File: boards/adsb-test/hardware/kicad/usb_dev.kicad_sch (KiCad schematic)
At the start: 108 parts, among them J1001 Dev USB-C, Q1001 MMBT3904, Q1002 MMBT3904, Q1003 MMBT3904, Q1004 MMBT3904, SW1001 BOOTSEL (programmer), U1001 USBLC6-2SC6, U1002 AP2112K-3.3, U1003 USB2514B, U1004 FT2232HL, U1005 93LC56B, U1006 74LVC1G07, U1007 74LVC1G125, U1008 74LVC1G07, U1009 74LVC1G125, U1010 RP2040, U1011 W25Q16JVSS, U1012 74LVC1G125, U1013 74LVC1G125, U1014 74LVC1G125, U1015 74LVC1G125, Y1001 24MHz, Y1002 12MHz, Y1003 12MHz

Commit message: ADSB_Test: User USB-C on its own sheet, RP2040 GPIO header + optional I2C, shunt/PWR_FLAG text fixed
Co-Authored-By: Claude Opus 5.5 <noreply@anthropic.com>
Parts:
- added J1003: RP2040 GPIO (pins DNP), Connector_PinHeader_2.54mm:PinHeader_2x14_P2.54mm_Vertical, symbol Connector_Generic:Conn_02x14_Odd_Even
- added R1041, R1042: 0R, Resistor_SMD:R_0805_2012Metric_Pad1.20x1.40mm_HandSolder, symbol Device:R
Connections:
- net 3V3_DEV: now also J1003.1 (Pin_1)
- net GND: now also J1003.27 (Pin_27), J1003.28 (Pin_28)
- net RP_GPIO8: now reaches U1010.11 (GPIO8)
- net RP_GPIO8: now also J1003.10 (Pin_10)
- net RP_GPIO9: now reaches U1010.12 (GPIO9)
- net RP_GPIO9: now also J1003.11 (Pin_11)
- net RP_GPIO10: now reaches U1010.13 (GPIO10)
- net RP_GPIO10: now also J1003.12 (Pin_12)
- net RP_GPIO11: now reaches U1010.14 (GPIO11)
- net RP_GPIO11: now also J1003.13 (Pin_13)
- net RP_GPIO12: now reaches U1010.15 (GPIO12)
- net RP_GPIO12: now also J1003.14 (Pin_14)
- net RP_GPIO13: now reaches U1010.16 (GPIO13)
- net RP_GPIO13: now also J1003.15 (Pin_15)
- net RP_GPIO14: now reaches U1010.17 (GPIO14)
- net RP_GPIO14: now also J1003.16 (Pin_16)
- net RP_GPIO15: now reaches U1010.18 (GPIO15)
- net RP_GPIO15: now also J1003.17 (Pin_17)
- net RP_GPIO0: now reaches U1010.2 (GPIO0)
- net RP_GPIO0: now also J1003.2 (Pin_2), R1041.1
- net RP_GPIO17: now reaches U1010.28 (GPIO17)
- net RP_GPIO17: now also J1003.18 (Pin_18)
- net RP_GPIO18: now reaches U1010.29 (GPIO18)
- net RP_GPIO18: now also J1003.19 (Pin_19)
- net RP_GPIO1: now reaches U1010.3 (GPIO1)
- net RP_GPIO1: now also J1003.3 (Pin_3), R1042.1
- net RP_GPIO19: now reaches U1010.30 (GPIO19)
- net RP_GPIO19: now also J1003.20 (Pin_20)
- net RP_GPIO20: now reaches U1010.31 (GPIO20)
- net RP_GPIO20: now also J1003.21 (Pin_21)
- net RP_GPIO21: now reaches U1010.32 (GPIO21)
- net RP_GPIO21: now also J1003.22 (Pin_22)
- net RP_GPIO22: now reaches U1010.34 (GPIO22)
- net RP_GPIO22: now also J1003.23 (Pin_23)
- net RP_GPIO23: now reaches U1010.35 (GPIO23)
- net RP_GPIO23: now also J1003.24 (Pin_24)
- net RP_GPIO24: now reaches U1010.36 (GPIO24)
- net RP_GPIO24: now also J1003.25 (Pin_25)
- net RP_GPIO25: now reaches U1010.37 (GPIO25)
- net RP_GPIO25: now also J1003.26 (Pin_26)
- net RP_GPIO2: now reaches U1010.4 (GPIO2)
- net RP_GPIO2: now also J1003.4 (Pin_4)
- net RP_GPIO3: now reaches U1010.5 (GPIO3)
- net RP_GPIO3: now also J1003.5 (Pin_5)
- net RP_GPIO4: now reaches U1010.6 (GPIO4)
- net RP_GPIO4: now also J1003.6 (Pin_6)
- net RP_GPIO5: now reaches U1010.7 (GPIO5)
- net RP_GPIO5: now also J1003.7 (Pin_7)
- net RP_GPIO6: now reaches U1010.8 (GPIO6)
- net RP_GPIO6: now also J1003.8 (Pin_8)
- net RP_GPIO7: now reaches U1010.9 (GPIO7)
- net RP_GPIO7: now also J1003.9 (Pin_9)
- new net I2C_SCL: R1042.2
- new net I2C_SDA: R1041.2
- no-connect marks 66 -> 41

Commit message: ADSB_Test: Dev port split over three A3 sheets; old note boxes replaced with short current notes
Co-Authored-By: Claude Opus 5.5 <noreply@anthropic.com>
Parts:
- removed C1013, C1014, C1015, C1016, C1024, C1025, C1026, C1027, C1028, C1029, C1030, C1031, C1032, C1033, C1034, C1035, C1036, C1037: 100nF, Capacitor_SMD:C_0805_2012Metric_Pad1.18x1.45mm_HandSolder, symbol Device:C
- removed C1017: 4.7uF, Capacitor_SMD:C_0805_2012Metric_Pad1.18x1.45mm_HandSolder, symbol Device:C
- removed C1018, C1019, C1020, C1021: 27pF, Capacitor_SMD:C_0805_2012Metric_Pad1.18x1.45mm_HandSolder, symbol Device:C
- removed C1022, C1023: 1uF, Capacitor_SMD:C_0805_2012Metric_Pad1.18x1.45mm_HandSolder, symbol Device:C
- removed D1001: 1N4148W, Diode_SMD:D_SOD-123, symbol Device:D
- removed D1002: WS2812B, LED_SMD:LED_WS2812B_PLCC4_5.0x5.0mm_P3.2mm, symbol LED:WS2812B
- removed J1003: RP2040 GPIO (pins DNP), Connector_PinHeader_2.54mm:PinHeader_2x14_P2.54mm_Vertical, symbol Connector_Generic:Conn_02x14_Odd_Even
- removed Q1001, Q1002, Q1003, Q1004: MMBT3904, Package_TO_SOT_SMD:SOT-23_Handsoldering, symbol Transistor_BJT:MMBT3904
- removed R1014: 12k 1%, Resistor_SMD:R_0805_2012Metric_Pad1.20x1.40mm_HandSolder, symbol Device:R
- removed R1015, R1017, R1018, R1019, R1020, R1021, R1022, R1023, R1024, R1025, R1033, R1034, R1039: 10k, Resistor_SMD:R_0805_2012Metric_Pad1.20x1.40mm_HandSolder, symbol Device:R
- removed R1016: 2.2k, Resistor_SMD:R_0805_2012Metric_Pad1.20x1.40mm_HandSolder, symbol Device:R
- removed R1030, R1031: 27R, Resistor_SMD:R_0805_2012Metric_Pad1.20x1.40mm_HandSolder, symbol Device:R
- removed R1032, R1035: 1k, Resistor_SMD:R_0805_2012Metric_Pad1.20x1.40mm_HandSolder, symbol Device:R
- removed R1036: 330R, Resistor_SMD:R_0805_2012Metric_Pad1.20x1.40mm_HandSolder, symbol Device:R
- removed R1037, R1038, R1041, R1042: 0R, Resistor_SMD:R_0805_2012Metric_Pad1.20x1.40mm_HandSolder, symbol Device:R
- removed R1040: 100k, Resistor_SMD:R_0805_2012Metric_Pad1.20x1.40mm_HandSolder, symbol Device:R
- removed SW1001: BOOTSEL (programmer), Button_Switch_THT:SW_PUSH_6mm, symbol Switch:SW_Push
- removed TP1003: RP_SWCLK, TestPoint:TestPoint_Pad_D1.5mm, symbol Connector:TestPoint
- removed TP1004: RP_SWDIO, TestPoint:TestPoint_Pad_D1.5mm, symbol Connector:TestPoint
- removed TP1005: RP_RUN, TestPoint:TestPoint_Pad_D1.5mm, symbol Connector:TestPoint
- removed TP1006: FT_A_DTR, TestPoint:TestPoint_Pad_D1.5mm, symbol Connector:TestPoint
- removed TP1007: FT_A_RTS, TestPoint:TestPoint_Pad_D1.5mm, symbol Connector:TestPoint
- removed TP1008: FT_B_DTR, TestPoint:TestPoint_Pad_D1.5mm, symbol Connector:TestPoint
- removed TP1009: FT_B_RTS, TestPoint:TestPoint_Pad_D1.5mm, symbol Connector:TestPoint
- removed U1004: FT2232HL, Package_QFP:LQFP-64_10x10mm_P0.5mm, symbol Interface_USB:FT2232HL
- removed U1005: 93LC56B, Package_SO:SOIC-8_3.9x4.9mm_P1.27mm, symbol Memory_EEPROM:93LCxxB
- removed U1006, U1008: 74LVC1G07, Package_TO_SOT_SMD:SOT-23-5_HandSoldering, symbol 74xGxx:74LVC1G07
- removed U1007, U1009, U1012, U1013, U1014, U1015: 74LVC1G125, Package_TO_SOT_SMD:SOT-23-5_HandSoldering, symbol 74xGxx:74LVC1G125
- removed U1010: RP2040, ADSB_Test:QFN-56-1EP_7x7mm_P0.4mm_EP3.2x3.2mm_HandSolder, symbol MCU_RaspberryPi:RP2040
- removed U1011: W25Q16JVSS, Package_SO:SOIC-8_5.3x5.3mm_P1.27mm, symbol Memory_Flash:W25Q16JVSS
- removed Y1002, Y1003: 12MHz, Crystal:Crystal_SMD_5032-2Pin_5.0x3.2mm_HandSoldering, symbol Device:Crystal
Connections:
- no-connect marks 41 -> 10
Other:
- note added: "DEV PORT, page 1 of 3: Dev USB-C -> USBLC6 -> USB2514B hub (strap defaults, bus powered). Own 3V3_DEV domain from Dev VBUS (AP2112K), so the Dev port works with the target unpowered. Downstream: DN1 P4 USB-Serial/JTAG | DN2 disabled (the C5 USB pins are its SDIO bus) | DN3 FT2232H -> page 'Dev UARTs' | DN4 RP2040 -> page 'Dev m1421 Programmer'."
- note removed: "DEV PORT (own 3V3_DEV domain from Dev VBUS; works with the target unpowered): USB-C -> USBLC6 -> USB2514B hub (strap defaults, bus powered). DN1 P4 USB-Serial/JTAG, DN2 disabled (C5 USB = SDIO pins), DN3 FT2232HL: A = P4 UART0, B = C5 UART0, DTR/RTS -> MMBT3904 pairs (esptool auto-reset) on P4_EN/BOOT and C5_EN/BOOT. DN4 RP2040 + W25Q16 running the STOCK ADSBee 1421 Programmer: GPIO26 ~SRST, 27 S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"
- title: ADSB_Test - USB Dev -> ADSB_Test - Dev USB Hub

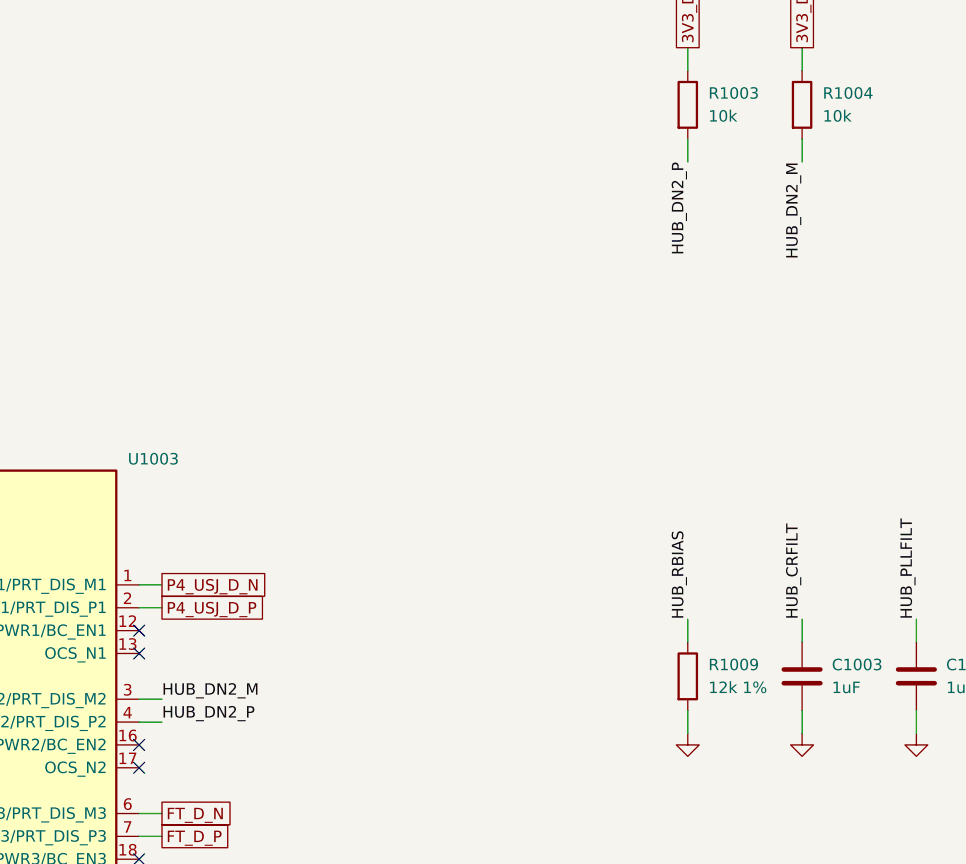
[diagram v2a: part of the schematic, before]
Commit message: ADSB_Test: Ethernet pairs named _P/_N, net classes restored in the project
- ETH_TXP/TXN/RXP/RXN -> ETH_TX_P/_N, ETH_RX_P/_N; HUB_DN2_M -> HUB_DN2_N.
- gen_pcb.py: pcbnew SaveBoard rewrote ADSB_Test.kicad_pro with empty
  net_settings, so every impedance class had been lost since the PCB start.
  Net settings are now kept across the save; 29 nets back in their classes.

Co-Authored-By: Claude Opus 5.5 <noreply@anthropic.com>
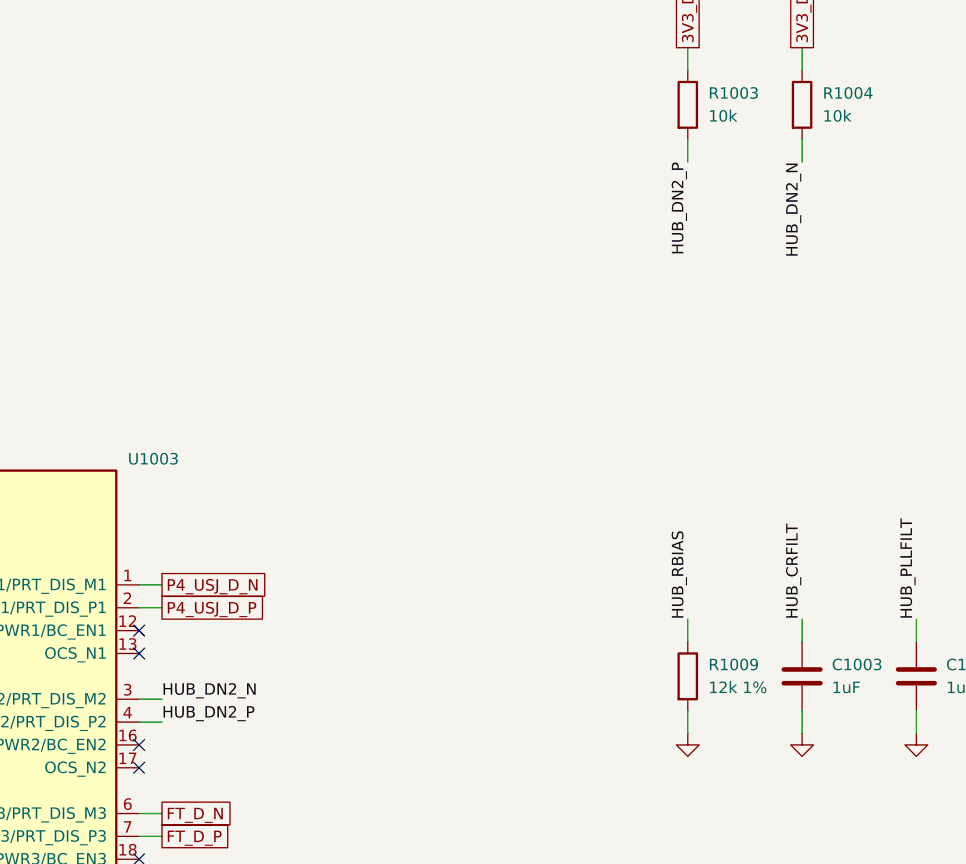
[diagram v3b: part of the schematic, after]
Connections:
- net HUB_DN2_M renamed HUB_DN2_N
